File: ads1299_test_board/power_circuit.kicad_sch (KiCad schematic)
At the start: 18 parts, among them IC1 TPS61023DRLR, IC2 TPS7A2030PDBVR, J1 Conn_01x02, SW1 SW_Push, U6 AP2112K-3.3

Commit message: 27/05
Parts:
- removed IC1: TPS61023DRLR, SOTFL50P160X60-6N, symbol TPS61023DRLR:TPS61023DRLR
- removed IC2: TPS7A2030PDBVR, SOT95P280X145-5N, symbol TPS7A2030PDBVR:TPS7A2030PDBVR
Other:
- moved on the sheet: R13

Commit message: charger circuit
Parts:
- removed F1: Fuse, symbol Device:Fuse
- removed J1: Conn_01x02, symbol Connector_Generic:Conn_01x02
- added IC1: TPS61023DRLR, SOTFL50P160X60-6N, symbol TPS61023DRLR:TPS61023DRLR
- added IC2: TPS7A2050PDBVR, SOT95P280X145-5N, symbol TPS7A2050PDBVR:TPS7A2050PDBVR
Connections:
- net +BATT is gone; now on net Vbat: SW1.2
- net agnd is gone; now on net GND: R13.1
- net +5V: now also IC2.5 (OUT)
- net SW: now also IC1.5 (SW)
- net VCC: now also IC1.6 (VOUT), IC2.1 (IN)
- net at R15.2: now also IC1.2 (EN)
- net at R17.1: now also IC2.3 (EN)
- net at C15.2, R14.1, R16.2: now also IC1.1 (FB)
- net Vbat: now reaches C16.1, L2.1
- net Vbat: now also IC1.3 (VIN)
- net -BATT renamed GND
- net GND: now also IC1.4 (GND), IC2.2 (GND); no longer U6.2 (GND)
- net dgnd renamed GNDD
- net GNDD: now also U6.2 (GND)
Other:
- moved on the sheet: C15, C16, C17, C18, C19, L2, R13, R14, R15, R16, R17, R18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

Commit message: usb, esp32 s3 wroom 1
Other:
- moved on the sheet: C15, C16, C17, C18, C19, IC1, IC2, L2, R13, R14, R15, R16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

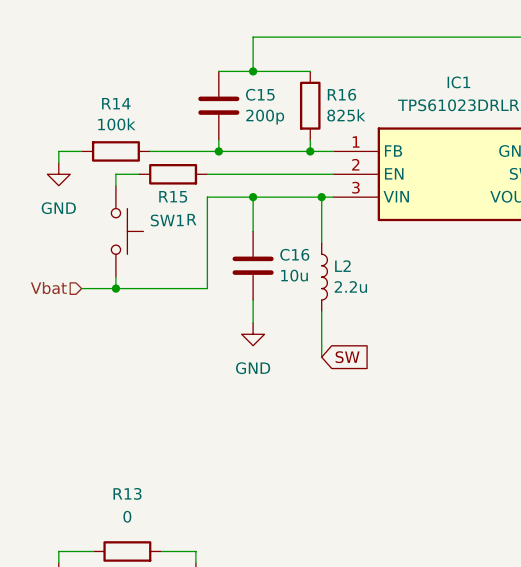
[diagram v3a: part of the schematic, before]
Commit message: usb charge and power circuit switch
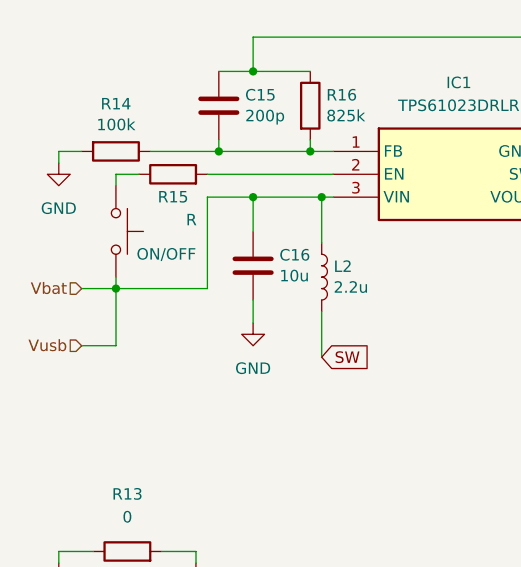
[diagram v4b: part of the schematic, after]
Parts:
- renumbered SW1 to ON/OFF
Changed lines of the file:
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@@
+	(wire
+		(pts
+			(xy 78.74 101.6) (xy 82.55 101.6)
+		)
+		(stroke
+			(width 0)
+			(type default)
+		)
+	)
 	(wire
 		(pts
@@
 		(pts
 			(xy 91.44 124.46) (xy 87.63 124.46)
+		)
+		(stroke
+			(width 0)
+			(type default)
+		)
+	)
+	(wire
+		(pts
+			(xy 82.55 101.6) (xy 82.55 95.25)
 		)
 		(stroke
@@
 				)
 			)
+		)
+	)
+	(hierarchical_label "Vusb"
+		(shape input)
+		(at 78.74 101.6 180)
+		(effects
+			(font
+				(size 1.27 1.27)
+			)
+			(justify right)
 		)
 	)
@@
 		(in_pos_files yes)
 		(dnp no)
-		(property "Reference" "SW1"
-			(at 86.3092 87.7316 90)
+		(property "Reference" "ON/OFF"
+			(at 84.836 91.44 90)
 			(show_name no)
 			(do_not_autoplace no)
@@
 			(project "ads1299_test_board"
 				(path "/97f9a33a-d3bd-406a-9672-b92babffe6b5/a537b4c0-2d82-4fbb-91d8-e3a7ef64a59b"
-					(reference "SW1")
+					(reference "ON/OFF")
 					(unit 1)
 				)

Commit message: GPIO, SRB
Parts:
- renumbered ON/OFF to ON/OFF1
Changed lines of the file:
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@@
 		(in_pos_files yes)
 		(dnp no)
-		(property "Reference" "ON/OFF"
+		(property "Reference" "ON/OFF1"
 			(at 84.836 91.44 90)
 			(show_name no)
@@
 			(project "ads1299_test_board"
 				(path "/97f9a33a-d3bd-406a-9672-b92babffe6b5/a537b4c0-2d82-4fbb-91d8-e3a7ef64a59b"
-					(reference "ON/OFF")
+					(reference "ON/OFF1")
 					(unit 1)
 				)

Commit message: updates
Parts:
- C15: value 200p -> 200pF; footprint (none) -> Capacitor_SMD:C_0402_1005Metric_Pad0.74x0.62mm_HandSolder
- C16: value 10u -> 10uF; footprint (none) -> Capacitor_SMD:C_0402_1005Metric_Pad0.74x0.62mm_HandSolder
- C17, C18, C19: value 20u -> 20uF; footprint (none) -> Capacitor_SMD:C_0805_2012Metric_Pad1.18x1.45mm_HandSolder
- IC1: footprint SOTFL50P160X60-6N -> Package_TO_SOT_SMD:SOT-563
- IC2: footprint SOT95P280X145-5N -> Package_TO_SOT_SMD:SOT-23-5_HandSoldering
- L2: value 2.2u -> 2.2uH; footprint (none) -> Inductor_SMD:L_Wuerth_HCI-5040
- R14, R16: footprint (none) -> Resistor_SMD:R_0402_1005Metric_Pad0.72x0.64mm_HandSolder
- R15, R18: value R -> 10k; footprint (none) -> Resistor_SMD:R_0402_1005Metric_Pad0.72x0.64mm_HandSolder
- R17: value R -> 10K; footprint (none) -> Resistor_SMD:R_0402_1005Metric_Pad0.72x0.64mm_HandSolder
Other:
- moved on the sheet: C17
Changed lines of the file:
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@@
 	(paper "A4")
 	(junction
+		(at 134.62 85.09)
+		(diameter 0)
+		(color 0 0 0 0)
+	)
+	(junction
 		(at 97.79 71.12)
 		(diameter 0)
@@
 	)
 	(junction
-		(at 134.62 85.09)
-		(diameter 0)
-		(color 0 0 0 0)
-	)
-	(junction
 		(at 104.14 80.01)
 		(diameter 0)
@@
 	(wire
 		(pts
-			(xy 134.62 96.52) (xy 134.62 99.06)
+			(xy 134.62 97.79) (xy 134.62 99.06)
 		)
 		(stroke
@@
 	(wire
 		(pts
-			(xy 134.62 88.9) (xy 134.62 85.09)
+			(xy 134.62 90.17) (xy 134.62 85.09)
 		)
 		(stroke
@@
 	(symbol
 		(lib_id "Device:C")
-		(at 134.62 92.71 0)
+		(at 134.62 93.98 0)
 		(unit 1)
 		(body_style 1)
@@
 		(dnp no)
 		(property "Reference" "C17"
-			(at 137.541 91.5416 0)
+			(at 137.541 92.8116 0)
 			(show_name no)
 			(do_not_autoplace no)
@@
 			)
 		)
-		(property "Value" "20u"
-			(at 137.541 93.853 0)
+		(property "Value" "20uF"
+			(at 137.541 95.123 0)
 			(show_name no)
 			(do_not_autoplace no)
@@
 			)
 		)
-		(property "Footprint" ""
-			(at 135.5852 96.52 0)
+		(property "Footprint" "Capacitor_SMD:C_0805_2012Metric_Pad1.18x1.45mm_HandSolder"
+			(at 135.5852 97.79 0)
 			(hide yes)
 			(show_name no)
@@
 		)
 		(property "Datasheet" "~"
-			(at 134.62 92.71 0)
+			(at 134.62 93.98 0)
 			(hide yes)
 			(show_name no)
@@
 		)
 		(property "Description" ""
-			(at 134.62 92.71 0)
+			(at 134.62 93.98 0)
 			(show_name no)
 			(do_not_autoplace no)
@@
 			)
 		)
-		(property "Value" "R"
-			(at 90.932 87.63 90)
+		(property "Value" "10k"
+			(at 88.9 87.376 90)
 			(show_name no)
 			(do_not_autoplace no)
@@
 			)
 		)
-		(property "Footprint" ""
+		(property "Footprint" "Resistor_SMD:R_0402_1005Metric_Pad0.72x0.64mm_HandSolder"
 			(at 88.9 84.328 90)
 			(hide yes)
@@
 			)
 		)
-		(property "Value" "R"
+		(property "Value" "10K"
 			(at 187.96 115.1636 90)
 			(show_name no)
@@
 			)
 		)
-		(property "Footprint" ""
+		(property "Footprint" "Resistor_SMD:R_0402_1005Metric_Pad0.72x0.64mm_HandSolder"
 			(at 190.5 116.332 90)
 			(hide yes)
@@
 			)
 		)
-		(property "Value" "20u"
+		(property "Value" "20uF"
 			(at 154.051 95.123 0)
 			(show_name no)
@@
 			)
 		)
-		(property "Footprint" ""
+		(property "Footprint" "Capacitor_SMD:C_0805_2012Metric_Pad1.18x1.45mm_HandSolder"
 			(at 152.0952 97.79 0)
 			(hide yes)
@@
 			)
 		)
-		(property "Value" "200p"
+		(property "Value" "200pF"
 			(at 96.901 76.073 0)
 			(show_name no)
@@
 			)
 		)
-		(property "Footprint" ""
+		(property "Footprint" "Capacitor_SMD:C_0402_1005Metric_Pad0.74x0.62mm_HandSolder"
 			(at 94.9452 78.74 0)
 			(hide yes)
@@
 			)
 		)
-		(property "Footprint" ""
+		(property "Footprint" "Resistor_SMD:R_0402_1005Metric_Pad0.72x0.64mm_HandSolder"
 			(at 102.362 74.93 90)
 			(hide yes)
@@
 			)
 		)
-		(property "Footprint" "SOT95P280X145-5N"
+		(property "Footprint" "Package_TO_SOT_SMD:SOT-23-5_HandSoldering"
 			(at 220.98 200.33 0)
 			(hide yes)
@@
 			)
 		)
-		(property "Value" "2.2u"
+		(property "Value" "2.2uH"
 			(at 106.7308 95.123 0)
 			(show_name no)
@@
 			)
 		)
-		(property "Footprint" ""
+		(property "Footprint" "Inductor_SMD:L_Wuerth_HCI-5040"
 			(at 105.41 93.98 0)
 			(hide yes)
@@
 			)
 		)
-		(property "Description" ""
+		(property "Description" "744316220"
 			(at 105.41 93.98 0)
+			(hide yes)
 			(show_name no)
 			(do_not_autoplace no)
@@
 			)
 		)
-		(property "Value" "20u"
+		(property "Value" "20uF"
 			(at 170.561 95.123 0)
 			(show_name no)
@@
 			)
 		)
-		(property "Footprint" ""
+		(property "Footprint" "Capacitor_SMD:C_0805_2012Metric_Pad1.18x1.45mm_HandSolder"
 			(at 168.6052 97.79 0)
 			(hide yes)
@@
 			)
 		)
-		(property "Footprint" "SOTFL50P160X60-6N"
+		(property "Footprint" "Package_TO_SOT_SMD:SOT-563"
 			(at 130.81 174.93 0)
 			(hide yes)
@@
 			)
 		)
-		(property "Footprint" ""
+		(property "Footprint" "Resistor_SMD:R_0402_1005Metric_Pad0.72x0.64mm_HandSolder"
 			(at 82.55 78.232 90)
 			(hide yes)
@@
 			)
 		)
-		(property "Value" "10u"
+		(property "Value" "10uF"
 			(at 100.711 93.853 0)
 			(show_name no)
@@
 			)
 		)
-		(property "Footprint" ""
+		(property "Footprint" "Capacitor_SMD:C_0402_1005Metric_Pad0.74x0.62mm_HandSolder"
 			(at 98.7552 96.52 0)
 			(hide yes)
@@
 			)
 		)
-		(property "Value" "R"
+		(property "Value" "10k"
 			(at 195.58 71.9836 90)
 			(show_name no)
@@
 			)
 		)
-		(property "Footprint" ""
+		(property "Footprint" "Resistor_SMD:R_0402_1005Metric_Pad0.72x0.64mm_HandSolder"
 			(at 195.58 73.152 90)
 			(hide yes)

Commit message: fixed Vbat net name
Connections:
- net Vbat renamed Vbat_out
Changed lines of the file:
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@@
 		)
 	)
-	(hierarchical_label "Vbat"
+	(hierarchical_label "Vbat_out"
 		(shape input)
 		(at 78.74 95.25 180)
